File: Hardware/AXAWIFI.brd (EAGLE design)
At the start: 94 x 27.9 mm, 25 parts, among them IC1 MCP2003, J1 ESPROG-SOCKET, SW1 RESET, SW2 REFLASH

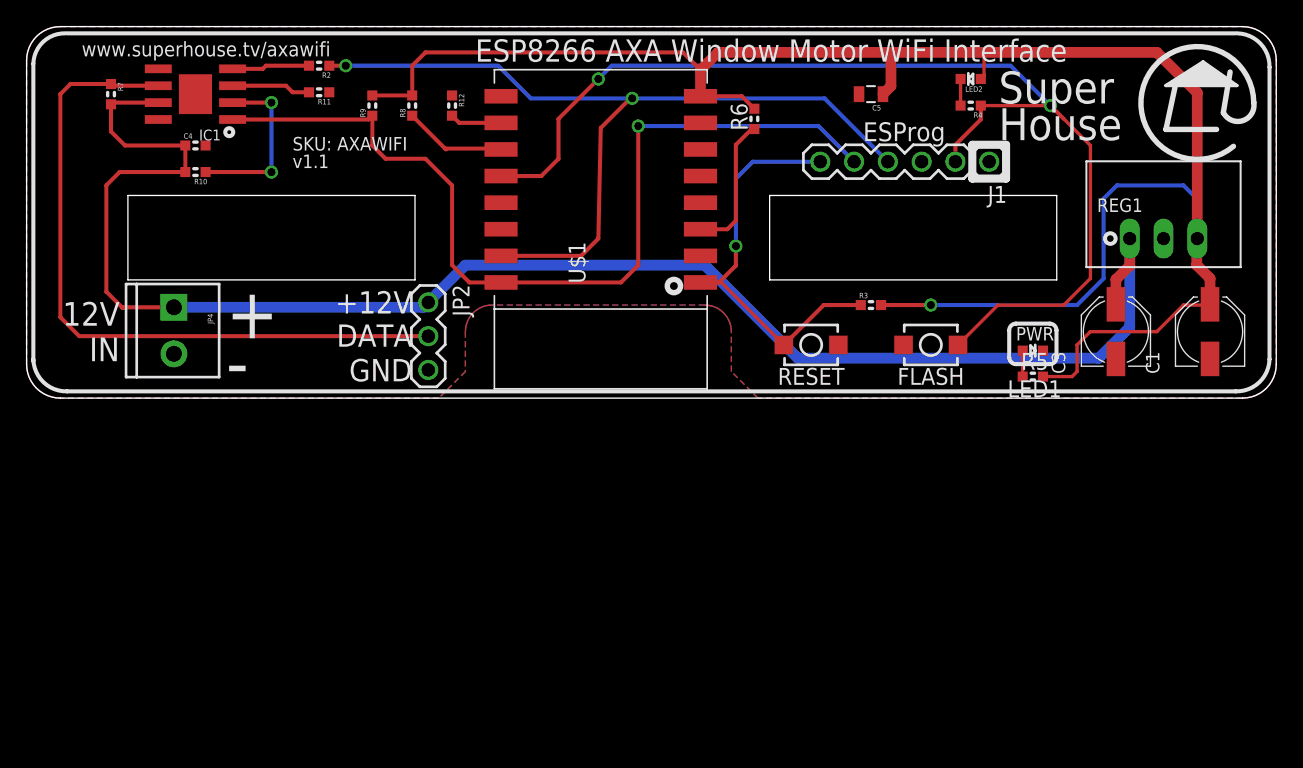
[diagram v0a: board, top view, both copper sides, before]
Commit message: Replaced obsolete programming header with ESPFlash header. Set MCP2003 to be permanently awake. Set MCP2003 to be deselected unless explicitly selected. Major restructure of schematic. Replaced parts using latest SuperHouse Eagle libraries to add 3D models.
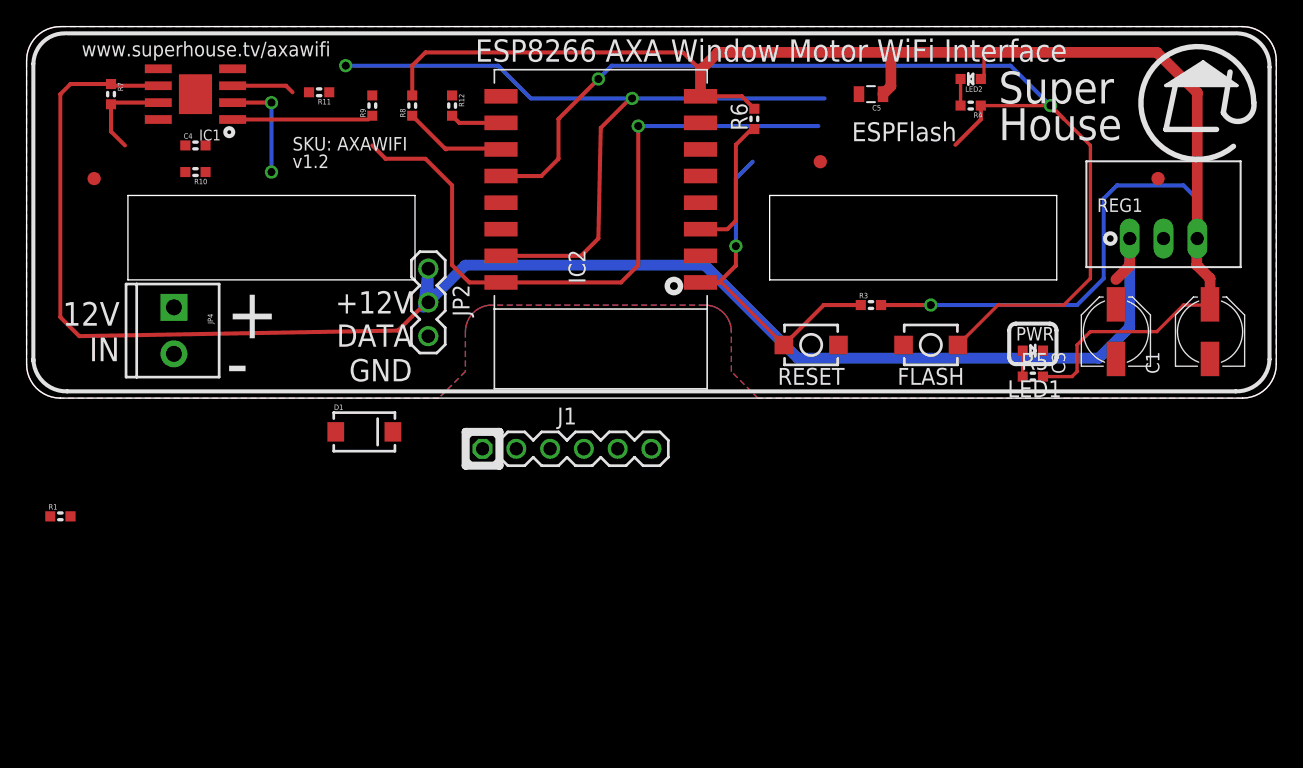
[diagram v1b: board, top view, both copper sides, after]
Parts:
- removed R2: 1K, SuperHouse-DiscreteSemi:R0603
- added D1: SS56, SuperHouse-Diodes:SMA-DIODE
- added FID1, FID2, FID3: FIDUCIAL1X2.5, SuperHouse-Symbols:FIDUCIAL-1X2.5
- added R1: 1K, SuperHouse-Resistors:R0603
- C1, C3: device SuperHouse-DiscreteSemi:PANASONIC_C -> SuperHouse-Capacitors:PANASONIC_C
- C4: device SuperHouse-DiscreteSemi:C0603 -> SuperHouse-Capacitors:C0603
- C5: device SuperHouse-DiscreteSemi:C0805 -> SuperHouse-Capacitors:C0805
- J1: value ESPROG-SOCKET -> ESPFLASH-1X6-2.54-SOCKET; device SuperHouse-Connectors:ESPROG-S -> SuperHouse-ESPFlash:1X6-2.54-SOCKET
- R10, R11, R12, R3, R4, R5, R6, R7, R8, R9: device SuperHouse-DiscreteSemi:R0603 -> SuperHouse-Resistors:R0603
- SW2: value REFLASH -> FLASH
- moved J1 38.4 mm to (40.6, -3.81), turned to 0 degrees
- renumbered U$1 to IC2
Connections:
- net GPIO12 renamed IO12
- net GPIO13 renamed IO13
- net GPIO14 renamed IO14
- net GPIO16 renamed IO16
- net GPIO4 renamed IO4
- net GPIO5 renamed IO5
- net N$6 renamed !LIN_WAKE
- removed net GPIO0: IC2.12, J1.2, R4.1, SW2.2
- removed net LINTX: IC1.4, R2.2
- removed net N$5: IC1.2, R10.1
- removed net RX: IC2.15, J1.4, R2.1
- removed net TX: IC1.1, IC2.16, J1.5, R9.1
- new net ESP_RX: IC2.15, J1.3, R1.1
- new net IO0: IC2.12, J1.6, R4.1, SW2.2
- new net LIN_CS: IC1.2, R10.2
- new net LIN_RX: IC1.1, IC2.16, J1.2, R9.1
- new net N$1: D1.A, JP4.1
- new net N$2: IC1.4, R1.2
- net !RST: now also J1.5; no longer J1.6
- net 12V: now also D1.C; no longer JP4.1, R10.2
- net 3.3V: now also J1.4; no longer J1.3
- net GND: now also R10.1
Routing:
- net GPIO0: track 84.3 -> 0.00 mm, vias 2 -> 0
- net IO0: track 0.00 -> 83.0 mm, vias 0 -> 2
- net TX: track 69.2 -> 0.00 mm, vias 1 -> 0
- net RX: track 64.5 -> 0.00 mm, vias 2 -> 0
- net LIN_RX: track 0.00 -> 62.6 mm, vias 0 -> 1
- net ESP_RX: track 0.00 -> 56.5 mm, vias 0 -> 2
- net 12V: track 122.7 -> 80.6 mm
- net N$5: track 13.1 -> 0.00 mm, vias 2 -> 0
- net LIN_CS: track 0.00 -> 8.15 mm, vias 0 -> 2
- net LINTX: track 5.84 -> 0.00 mm
- net !RST: track 30.5 -> 25.4 mm
- net 3.3V: track 145.7 -> 142.7 mm
- net !LIN_WAKE: track 5.95 -> 4.71 mm
- net DATA: track 52.8 -> 53.7 mm
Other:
- board text added: "ESPFlash"
- board text added: "SKU: AXAWIFI v1.2"
- board text removed: "ESProg"
- board text removed: "SKU: AXAWIFI v1.1"

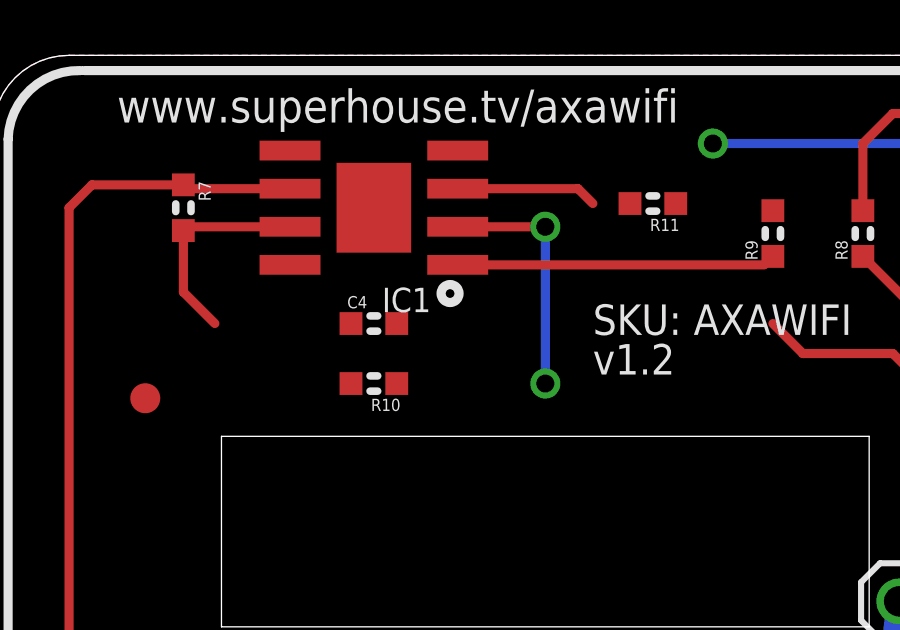
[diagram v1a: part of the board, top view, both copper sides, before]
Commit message: Assigned IO15 as LIN_CS.
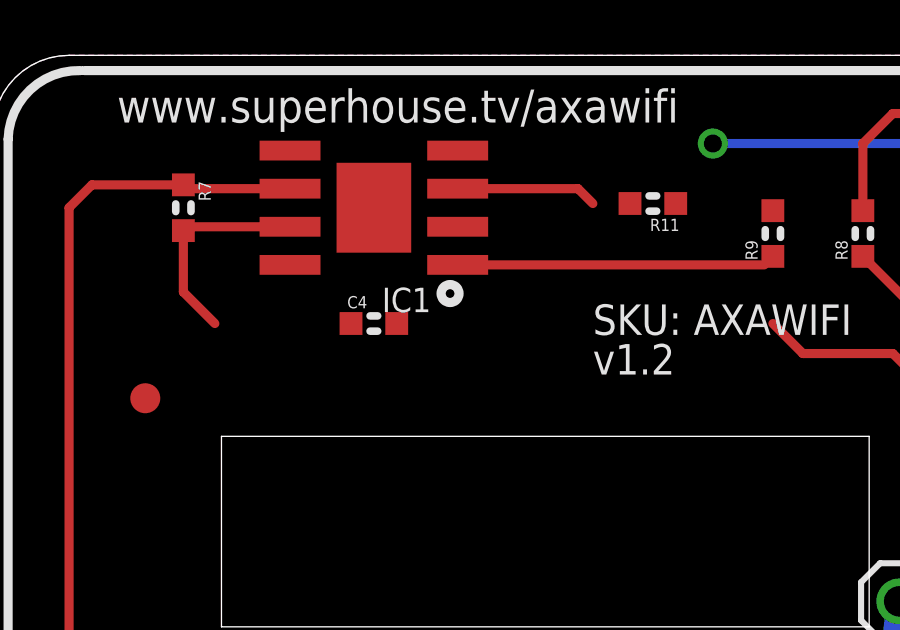
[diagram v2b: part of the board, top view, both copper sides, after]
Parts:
- removed R10: 22K, SuperHouse-Resistors:R0603
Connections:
- net IO4 renamed IO4_SDA
- net IO5 renamed IO5_SCL
- removed net LIN_CS: IC1.2, R10.2
- net GND: no longer R10.1
- net GPIO15: now also IC1.2
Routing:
- net LIN_CS: track 8.15 -> 0.00 mm, vias 2 -> 0
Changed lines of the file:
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@@
 <attribute name="VALUE" x="24.984" y="23.0348" size="1.016" layer="27" font="vector"/>
-</element>
-<element name="R10" library="SuperHouse-Resistors" library_urn="urn:adsk.eagle:library:28961094" package="R0603" package3d_urn="urn:adsk.eagle:package:28961141/1" value="22K" x="12.7" y="17" smashed="yes" rot="R180">
-<attribute name="NAME" x="13.589" y="16.492" size="0.4064" layer="25" font="vector" rot="R180"/>
-<attribute name="VALUE" x="9.284" y="17.0348" size="1.016" layer="27" font="vector"/>
 </element>
 <element name="R11" library="SuperHouse-Resistors" library_urn="urn:adsk.eagle:library:28961094" package="R0603" package3d_urn="urn:adsk.eagle:package:28961141/1" value="22K" x="22" y="23" smashed="yes" rot="R180">
@@
 <contactref element="C3" pad="-"/>
 <contactref element="C4" pad="2"/>
-<contactref element="R10" pad="1"/>
 <contactref element="R11" pad="1"/>
 <wire x1="89" y1="2.95" x2="85.5" y2="12" width="0" layer="19" extent="1-1"/>
@@
 <wire x1="9.906" y1="24.765" x2="12.7" y2="22.86" width="0" layer="19" extent="1-1"/>
 <wire x1="13.462" y1="19" x2="12.7" y2="22.86" width="0" layer="19" extent="1-1"/>
-<wire x1="13.462" y1="17" x2="13.462" y2="19" width="0" layer="19" extent="1-1"/>
-<wire x1="11.08" y1="3.33" x2="13.462" y2="17" width="0" layer="19" extent="1-1"/>
+<wire x1="11.08" y1="3.33" x2="13.462" y2="19" width="0" layer="19" extent="1-1"/>
 <wire x1="30.21" y1="4.66" x2="32" y2="22.762" width="0" layer="19" extent="1-1"/>
-<wire x1="34.29" y1="-3.81" x2="11.08" y2="3.33" width="0" layer="19" extent="1-1"/>
+<wire x1="34.29" y1="-3.81" x2="30.21" y2="4.66" width="0" layer="19" extent="1-1"/>
 </signal>
 <signal name="3.3V">
@@
 <wire x1="3.96" y1="4.66" x2="2.54" y2="6.08" width="0.3048" layer="1"/>
 </signal>
-<signal name="LIN_CS">
-<contactref element="IC1" pad="2"/>
-<wire x1="15.494" y1="22.225" x2="18.415" y2="22.225" width="0.3048" layer="1"/>
-<wire x1="18.415" y1="22.225" x2="18.415" y2="17" width="0.3048" layer="16"/>
-<via x="18.415" y="22.225" extent="1-16" drill="0.6"/>
-<via x="18.415" y="17" extent="1-16" drill="0.6"/>
-<contactref element="R10" pad="2"/>
-<wire x1="11.938" y1="17" x2="15.494" y2="22.225" width="0" layer="19" extent="1-1"/>
-</signal>
 <signal name="!LIN_WAKE">
 <contactref element="IC1" pad="3"/>
@@
 <contactref element="IC2" pad="10"/>
 <wire x1="32.538" y1="20.7" x2="35.68" y2="20.7" width="0.3048" layer="1"/>
+<contactref element="IC1" pad="2"/>
+<wire x1="15.494" y1="22.225" x2="32" y2="21.238" width="0" layer="19" extent="1-1"/>
 </signal>
 <signal name="!RST">
@@
 <wire x1="70.238" y1="22" x2="70.238" y2="24" width="0.254" layer="1"/>
 </signal>
-<signal name="IO4">
+<signal name="IO4_SDA">
 <contactref element="IC2" pad="14"/>
 </signal>
-<signal name="IO5">
+<signal name="IO5_SCL">
 <contactref element="IC2" pad="13"/>
 </signal>

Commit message: Rationalised part values and reordered designators.
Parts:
- added IC3: MCP9808-MSOP8, SuperHouse-Sensors:MSOP-8
- added LED3: GREEN, SuperHouse-LEDs:LED-0603
- added R10: 10K, SuperHouse-Resistors:R0603
- added R2: 1K, SuperHouse-Resistors:R0603
- C1: value 22uF 40V -> 100nF 50V; device SuperHouse-Capacitors:PANASONIC_C -> SuperHouse-Capacitors:C0603
- C4: value 100nF 50V -> 22uF 40V; device SuperHouse-Capacitors:C0603 -> SuperHouse-Capacitors:PANASONIC_C
- R11: value 22K -> 10K
- R3: value 10K -> 1K
- R4: value 1K -> 2K2
- R5: value 2K2 -> 4K7
- R6, R8: value 10K -> 4K7
- R9: value 4K7 -> 10K
- moved C1 77.6 mm to (12.7, 19.0), turned to 0 degrees
- moved C4 77.6 mm to (89.0, 5.00), turned to 90 degrees
- moved R5 72.5 mm to (6.35, 22.9), turned to 270 degrees
- moved R3 69.0 mm to (2.54, -25.4)
- moved R8 46.7 mm to (2.54, -16.5), turned to 0 degrees
- moved R7 42.1 mm to (2.54, -19.1), turned to 0 degrees
- moved R6 28.7 mm to (26.0, 22.0)
- moved R9 28.7 mm to (54.7, 21.0)
- moved R4 20.9 mm to (75.7, 1.62), turned to 0 degrees
- renumbered C5 to C2
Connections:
- new net N$3: LED3.C, R3.2
- net !RST: now also R10.1; no longer R3.1
- net 12V: now also C1.1, R5.2; no longer C4.1, R7.2
- net 3.3V: now also C4.+, IC3.8, LED3.A, R10.2, R4.2, R7.2; no longer C1.+, R3.2, R5.2
- net CH_PD: now also R9.1; no longer R6.1
- net DATA: now also R5.1; no longer R7.1
- net GND: now also C1.2, C4.-, IC3.4, IC3.5, IC3.6, IC3.7; no longer C1.-, C4.2
- net GPIO2: now also R3.1; no longer R8.1
- net IO0: now also R2.1; no longer R4.1
- net IO4_SDA: now also IC3.1, R8.1
- net IO5_SCL: now also IC3.2, R7.1
- net LIN_RX: now also R6.1; no longer R9.1
- net N$14: now also R4.1; no longer R5.1
- net N$20: now also R2.2; no longer R4.2
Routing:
- net GPIO2: track 7.83 -> 4.34 mm
- net 3.3V: track 142.7 -> 140.5 mm
